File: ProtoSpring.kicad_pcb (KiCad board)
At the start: 2 copper layers, 100 x 50 mm, 41 parts, among them P1 CONN_3X2, P10 CONN_14, P11 CONN_14, P12 CONN_14, P13 CONN_14, P14 CONN_14, P15 CONN_14, P16 CONN_14, P17 CONN_14, P18 CONN_14, P19 CONN_14, P2 CONN_7X2, P20 CONN_14, P21 CONN_14, P22 CONN_14, P23 CONN_14, P24 CONN_14, P25 CONN_14, P26 CONN_14, P27 CONN_14, P3 CONN_4X2, P4 CONN_3X2, P5 CONN_8X2, P6 CONN_2X2, P7 CONN_4X2, P8 CONN_14, P9 CONN_14

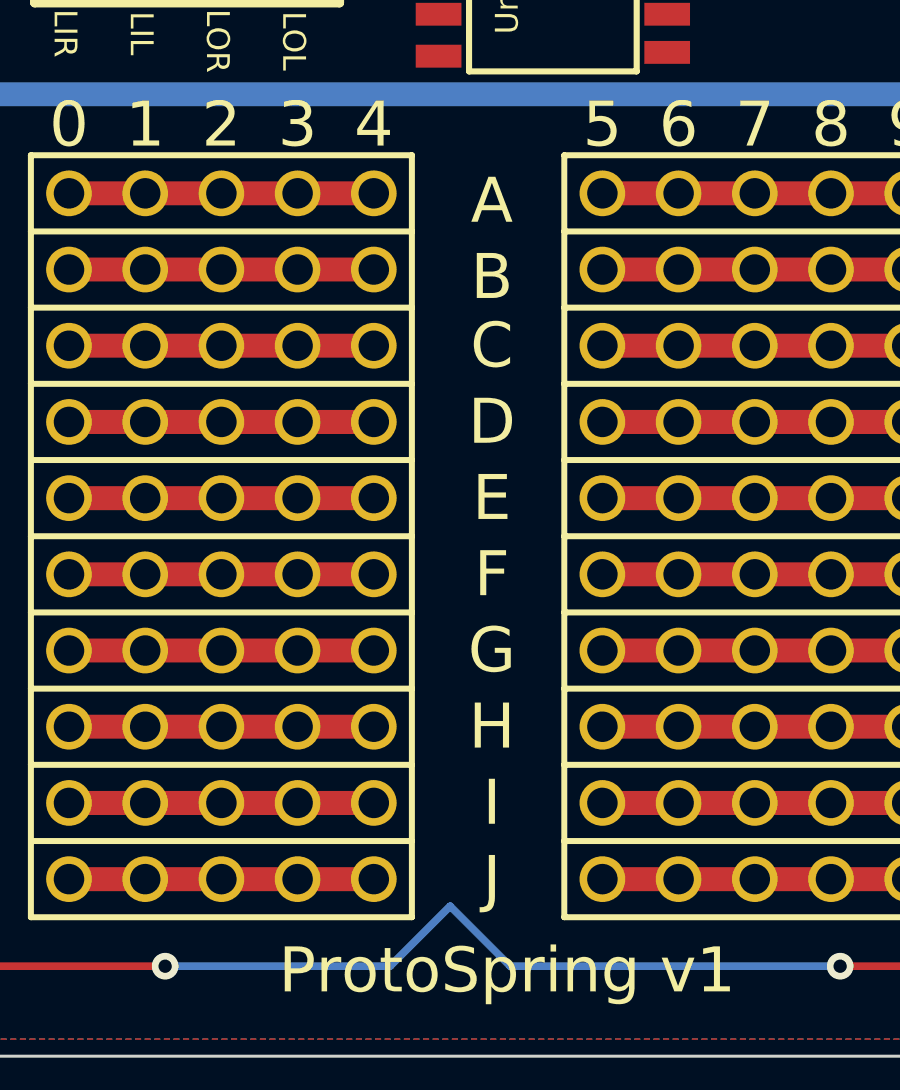
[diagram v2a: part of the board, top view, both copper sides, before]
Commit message: add missing path back for vias
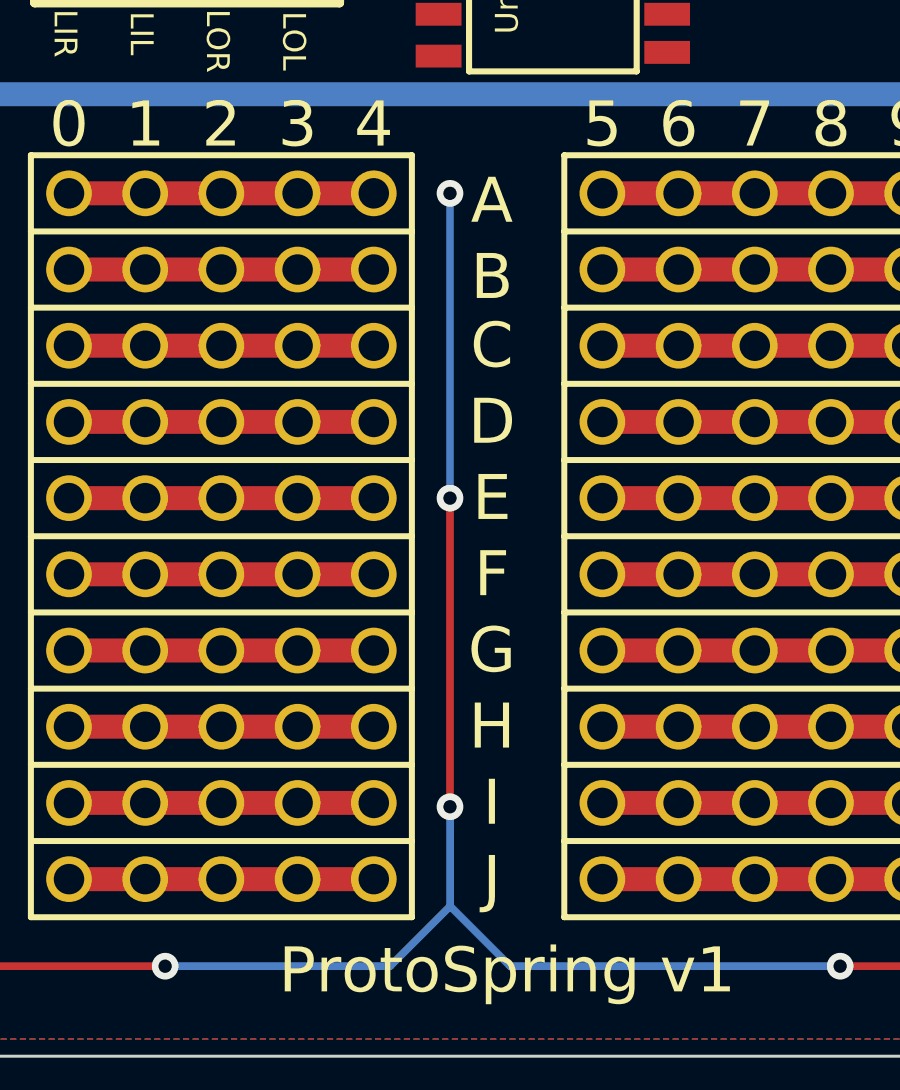
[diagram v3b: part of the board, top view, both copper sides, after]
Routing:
- net GND: track 209.7 -> 233.4 mm, vias 23 -> 26
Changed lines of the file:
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@@
     (thickness 1.6)
     (drawings 190)
-    (tracks 404)
+    (tracks 411)
     (zones 0)
     (modules 41)
@@
   (segment (start 139 110.552) (end 143.002 114.554) (width 0.254) (layer F.Cu) (net 19))
   (segment (start 214 108.5) (end 214 108.199) (width 0.254) (layer B.Cu) (net 20))
+  (segment (start 214 108.199) (end 215.138 107.061) (width 0.254) (layer B.Cu) (net 20))
+  (segment (start 215.138 107.061) (end 216.789 107.061) (width 0.254) (layer B.Cu) (net 20))
+  (segment (start 216.789 107.061) (end 219.202 109.474) (width 0.254) (layer B.Cu) (net 20))
+  (segment (start 219.202 109.474) (end 219.202 118.491) (width 0.254) (layer B.Cu) (net 20))
+  (segment (start 219.202 118.491) (end 218.567 119.126) (width 0.254) (layer B.Cu) (net 20))
+  (segment (start 218.567 119.126) (end 216.396 119.126) (width 0.254) (layer B.Cu) (net 20))
   (segment (start 216.396 119.126) (end 215 117.73) (width 0.254) (layer B.Cu) (net 20))
-  (segment (start 218.567 119.126) (end 216.396 119.126) (width 0.254) (layer B.Cu) (net 20))
-  (segment (start 219.202 118.491) (end 218.567 119.126) (width 0.254) (layer B.Cu) (net 20))
-  (segment (start 219.202 109.474) (end 219.202 118.491) (width 0.254) (layer B.Cu) (net 20))
-  (segment (start 216.789 107.061) (end 219.202 109.474) (width 0.254) (layer B.Cu) (net 20))
-  (segment (start 215.138 107.061) (end 216.789 107.061) (width 0.254) (layer B.Cu) (net 20))
-  (segment (start 214 108.199) (end 215.138 107.061) (width 0.254) (layer B.Cu) (net 20))
   (segment (start 210.566 114.046) (end 210.566 115.836) (width 0.254) (layer F.Cu) (net 21))
   (segment (start 210.566 108.966) (end 210.566 114.046) (width 0.254) (layer F.Cu) (net 21))
@@
   (segment (start 210.566 115.836) (end 212.46 117.73) (width 0.254) (layer F.Cu) (net 21))
   (segment (start 216 108.5) (end 216.45 108.5) (width 0.254) (layer B.Cu) (net 22))
+  (segment (start 216.45 108.5) (end 218.44 110.49) (width 0.254) (layer B.Cu) (net 22))
+  (segment (start 218.44 110.49) (end 218.44 116.83) (width 0.254) (layer B.Cu) (net 22))
   (segment (start 218.44 116.83) (end 217.54 117.73) (width 0.254) (layer B.Cu) (net 22))
-  (segment (start 218.44 110.49) (end 218.44 116.83) (width 0.254) (layer B.Cu) (net 22))
-  (segment (start 216.45 108.5) (end 218.44 110.49) (width 0.254) (layer B.Cu) (net 22))
+  (segment (start 150.5 150) (end 150.5 146.69) (width 0.254) (layer B.Cu) (net 23))
+  (via (at 150.495 126.238) (size 0.889) (layers F.Cu B.Cu) (net 23))
+  (segment (start 150.495 136.398) (end 150.495 126.238) (width 0.254) (layer B.Cu) (net 23))
+  (via (at 150.495 136.398) (size 0.889) (layers F.Cu B.Cu) (net 23))
+  (segment (start 150.495 146.685) (end 150.495 136.398) (width 0.254) (layer F.Cu) (net 23))
+  (via (at 150.495 146.685) (size 0.889) (layers F.Cu B.Cu) (net 23))
+  (segment (start 150.5 146.69) (end 150.495 146.685) (width 0.254) (layer B.Cu) (net 23))
   (segment (start 137.922 116.078) (end 131.572 116.078) (width 0.254) (layer F.Cu) (net 23))
   (via (at 131.572 116.078) (size 0.889) (layers F.Cu B.Cu) (net 23))

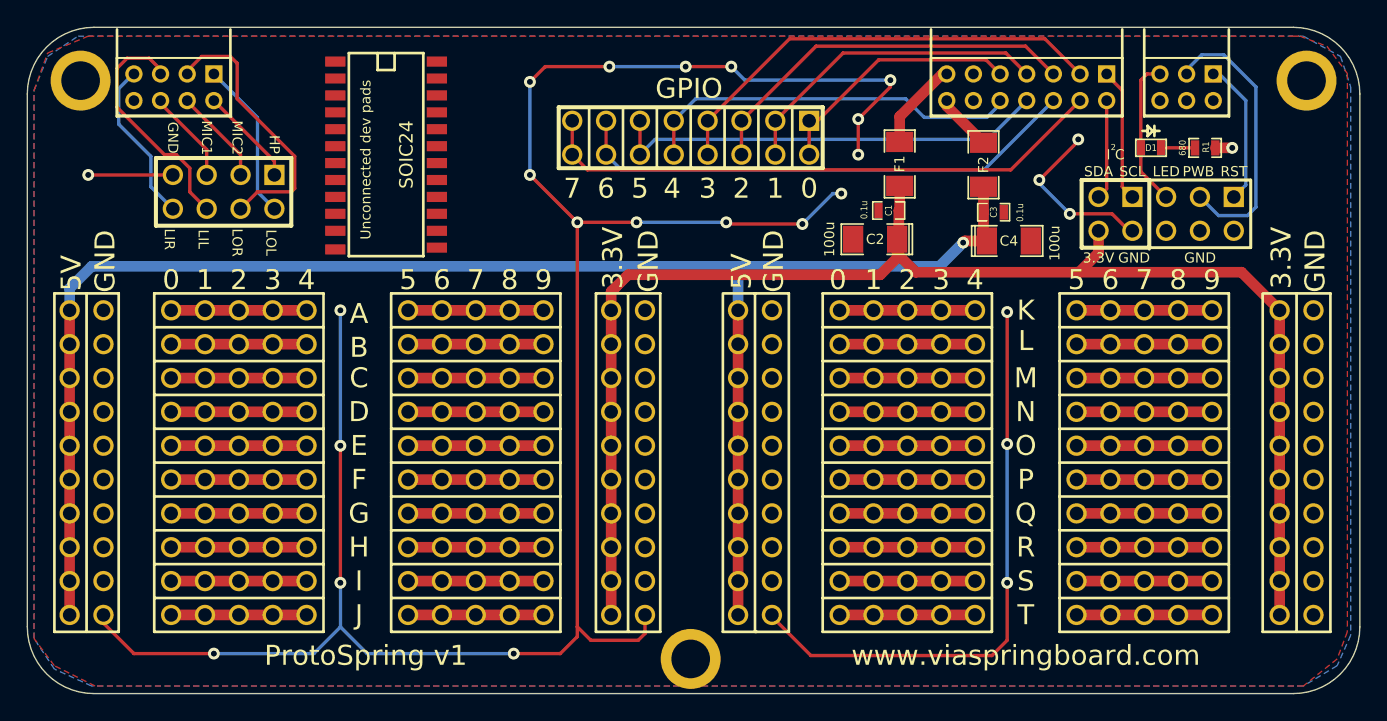
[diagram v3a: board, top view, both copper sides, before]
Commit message: bugfix: i2c lines labeling
The SDA and SCL lines were mixed up on the silkscreen. Fix their
labels and update version number on the board to reflect this change.
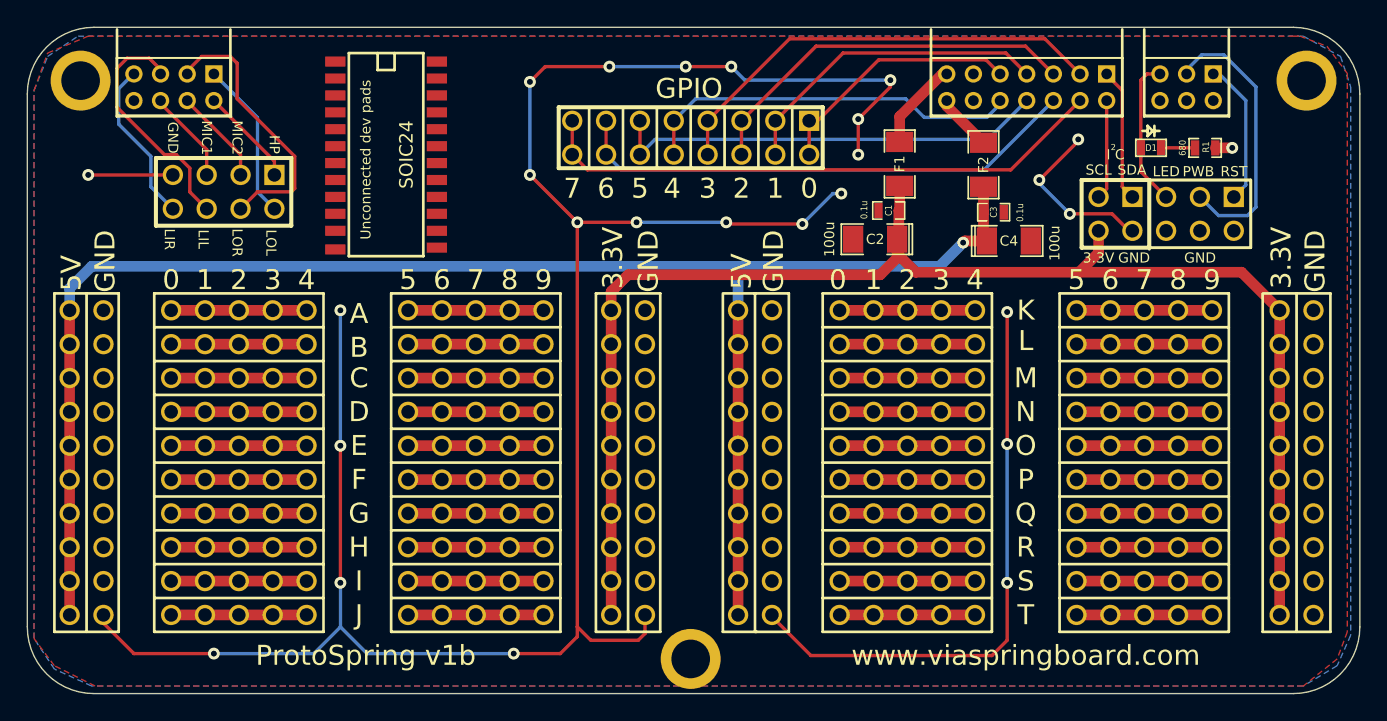
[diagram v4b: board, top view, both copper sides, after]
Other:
- board text added: "ProtoSpring v1b"
- board text removed: "ProtoSpring v1"
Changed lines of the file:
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@@
     (effects (font (size 0.762 0.762) (thickness 0.1905)))
   )
-  (gr_text SDA (at 207.391 115.824) (layer F.SilkS)
-    (effects (font (size 0.762 0.762) (thickness 0.1905)))
-  )
-  (gr_text SCL (at 209.931 115.824) (layer F.SilkS)
+  (gr_text SDA (at 209.9 115.7) (layer F.SilkS)
+    (effects (font (size 0.762 0.762) (thickness 0.1905)))
+  )
+  (gr_text SCL (at 207.4 115.7) (layer F.SilkS)
     (effects (font (size 0.762 0.762) (thickness 0.1905)))
   )
@@
     (effects (font (size 1.5 1.5) (thickness 0.3)))
   )
-  (gr_text "ProtoSpring v1" (at 152.4 152.146) (layer F.SilkS)
-    (effects (font (size 1.5 1.5) (thickness 0.3)))
-  )
+  (gr_text "ProtoSpring v1b" (at 152.4 152.146) (layer F.SilkS)
+    (effects (font (size 1.5 1.5) (thickness 0.3)))
+  )

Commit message: latest changes
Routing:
- net GND: track 233.4 -> 235.9 mm, vias 26 -> 27
- net /I2C0SCL: track 7.48 -> 8.26 mm
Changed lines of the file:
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@@
     (thickness 1.6)
     (drawings 190)
-    (tracks 411)
+    (tracks 417)
     (zones 0)
     (modules 41)
@@
   (segment (start 145.542 115.042) (end 145.542 116.078) (width 0.254) (layer F.Cu) (net 11))
   (segment (start 141 110.5) (end 145.542 115.042) (width 0.254) (layer F.Cu) (net 11))
-  (segment (start 208 117.12) (end 207.391 117.729) (width 0.254) (layer F.Cu) (net 12))
-  (segment (start 208 110.5) (end 208 117.12) (width 0.254) (layer F.Cu) (net 12))
+  (segment (start 208 110.5) (end 208 110.83) (width 0.254) (layer F.Cu) (net 12) (status C00000))
+  (segment (start 206.45 116.788) (end 207.391 117.729) (width 0.254) (layer F.Cu) (net 12) (status 800000))
+  (segment (start 206.45 112.38) (end 206.45 116.788) (width 0.254) (layer F.Cu) (net 12))
+  (segment (start 208 110.83) (end 206.45 112.38) (width 0.254) (layer F.Cu) (net 12) (status 400000))
   (segment (start 209.169 116.967) (end 209.931 117.729) (width 0.254) (layer F.Cu) (net 13))
   (segment (start 209.169 109.728) (end 209.169 116.967) (width 0.254) (layer F.Cu) (net 13))
@@
   (segment (start 218.44 110.49) (end 218.44 116.83) (width 0.254) (layer B.Cu) (net 22))
   (segment (start 218.44 116.83) (end 217.54 117.73) (width 0.254) (layer B.Cu) (net 22))
+  (segment (start 205.05 113.39) (end 207.75 113.39) (width 0.254) (layer B.Cu) (net 23))
+  (via (at 205.05 113.39) (size 0.889) (layers F.Cu B.Cu) (net 23))
+  (segment (start 205.05 113.517) (end 205.05 113.39) (width 0.254) (layer F.Cu) (net 23))
+  (segment (start 202.946 116.459) (end 205.05 113.517) (width 0.254) (layer F.Cu) (net 23))
+  (via (at 202.946 116.459) (size 0.889) (layers F.Cu B.Cu) (net 23))
+  (segment (start 202.946 116.713) (end 202.946 116.459) (width 0.254) (layer B.Cu) (net 23))
+  (segment (start 205.232 118.999) (end 202.946 116.713) (width 0.254) (layer B.Cu) (net 23))
+  (via (at 205.232 118.999) (size 0.889) (layers F.Cu B.Cu) (net 23))
+  (segment (start 208.407 118.999) (end 205.232 118.999) (width 0.254) (layer F.Cu) (net 23))
+  (segment (start 209.677 120.269) (end 208.407 118.999) (width 0.254) (layer F.Cu) (net 23))
+  (segment (start 209.931 120.269) (end 209.677 120.269) (width 0.254) (layer F.Cu) (net 23))
+  (segment (start 207.85 113.49) (end 207.85 113.41) (width 0.254) (layer F.Cu) (net 23))
+  (via (at 207.85 113.49) (size 0.889) (layers F.Cu B.Cu) (net 23))
+  (segment (start 207.75 113.39) (end 207.85 113.49) (width 0.254) (layer B.Cu) (net 23))
   (segment (start 150.5 150) (end 150.5 146.69) (width 0.254) (layer B.Cu) (net 23))
   (via (at 150.495 126.238) (size 0.889) (layers F.Cu B.Cu) (net 23))
@@
   (segment (start 172.72 119.634) (end 179.451 119.634) (width 0.254) (layer B.Cu) (net 23))
   (via (at 172.72 119.634) (size 0.889) (layers F.Cu B.Cu) (net 23))
-  (segment (start 209.931 120.269) (end 209.677 120.269) (width 0.254) (layer F.Cu) (net 23))
-  (via (at 205.867 113.411) (size 0.889) (layers F.Cu B.Cu) (net 23))
-  (segment (start 205.867 113.538) (end 205.867 113.411) (width 0.254) (layer F.Cu) (net 23))
-  (segment (start 202.946 116.459) (end 205.867 113.538) (width 0.254) (layer F.Cu) (net 23))
-  (via (at 202.946 116.459) (size 0.889) (layers F.Cu B.Cu) (net 23))
-  (segment (start 202.946 116.713) (end 202.946 116.459) (width 0.254) (layer B.Cu) (net 23))
-  (segment (start 205.232 118.999) (end 202.946 116.713) (width 0.254) (layer B.Cu) (net 23))
-  (via (at 205.232 118.999) (size 0.889) (layers F.Cu B.Cu) (net 23))
-  (segment (start 208.407 118.999) (end 205.232 118.999) (width 0.254) (layer F.Cu) (net 23))
-  (segment (start 209.677 120.269) (end 208.407 118.999) (width 0.254) (layer F.Cu) (net 23))
   (segment (start 189.357 114.554) (end 189.357 111.887) (width 0.254) (layer F.Cu) (net 23))
   (segment (start 191.77 108.966) (end 191.77 109.474) (width 0.254) (layer F.Cu) (net 23))
